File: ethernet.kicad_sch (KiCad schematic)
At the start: 48 parts

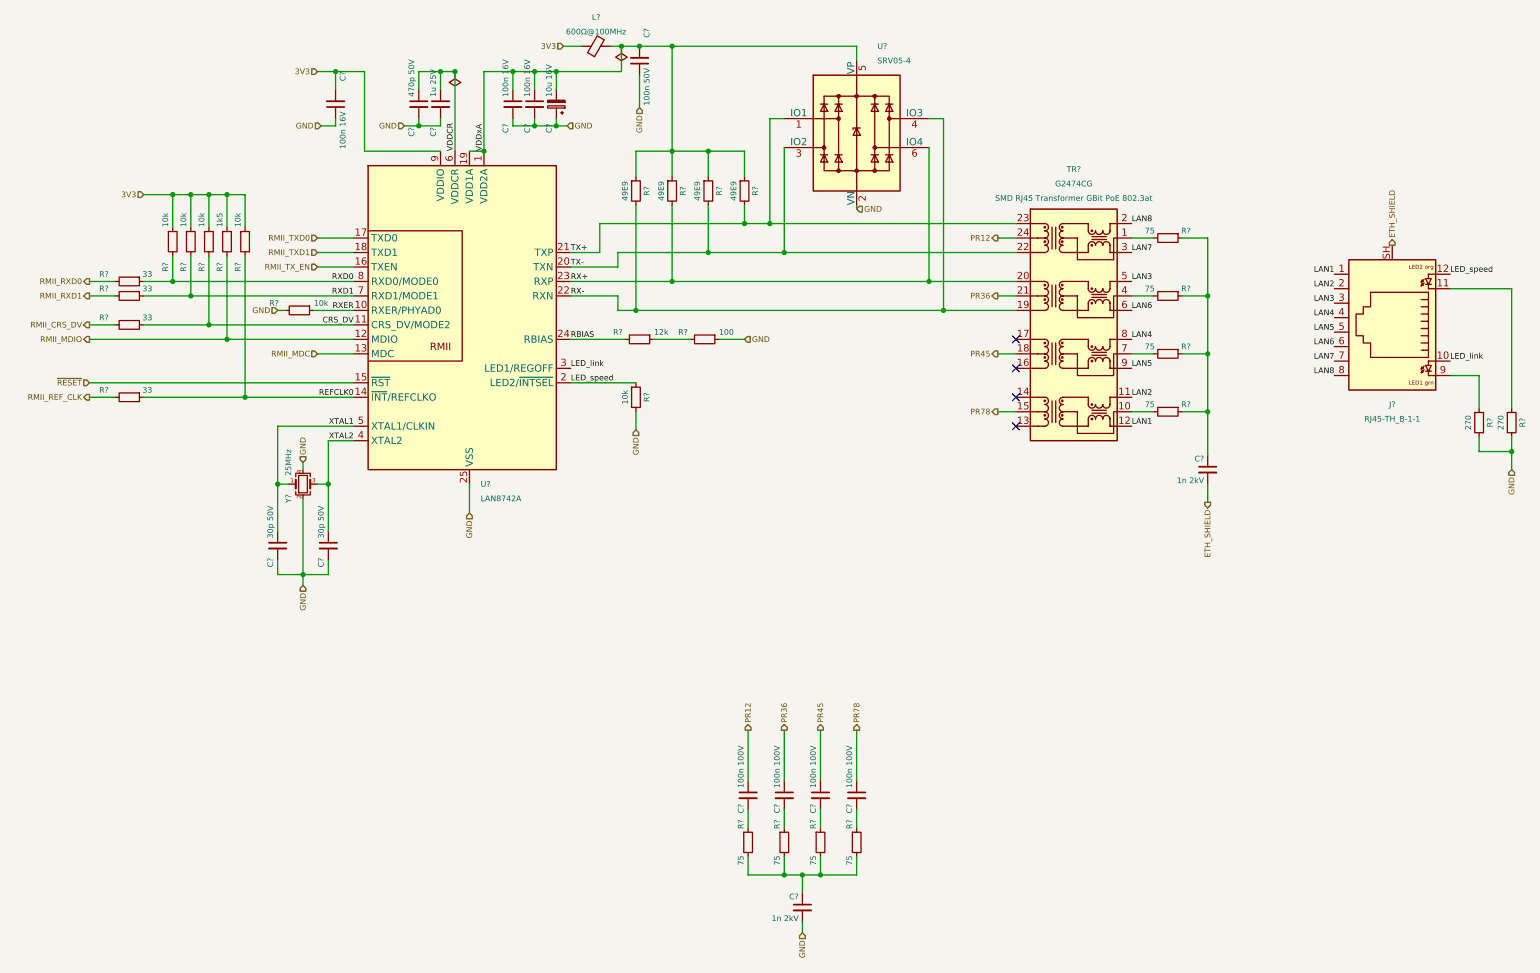
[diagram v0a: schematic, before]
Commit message: Replace transformer, replace RJ45 3D model
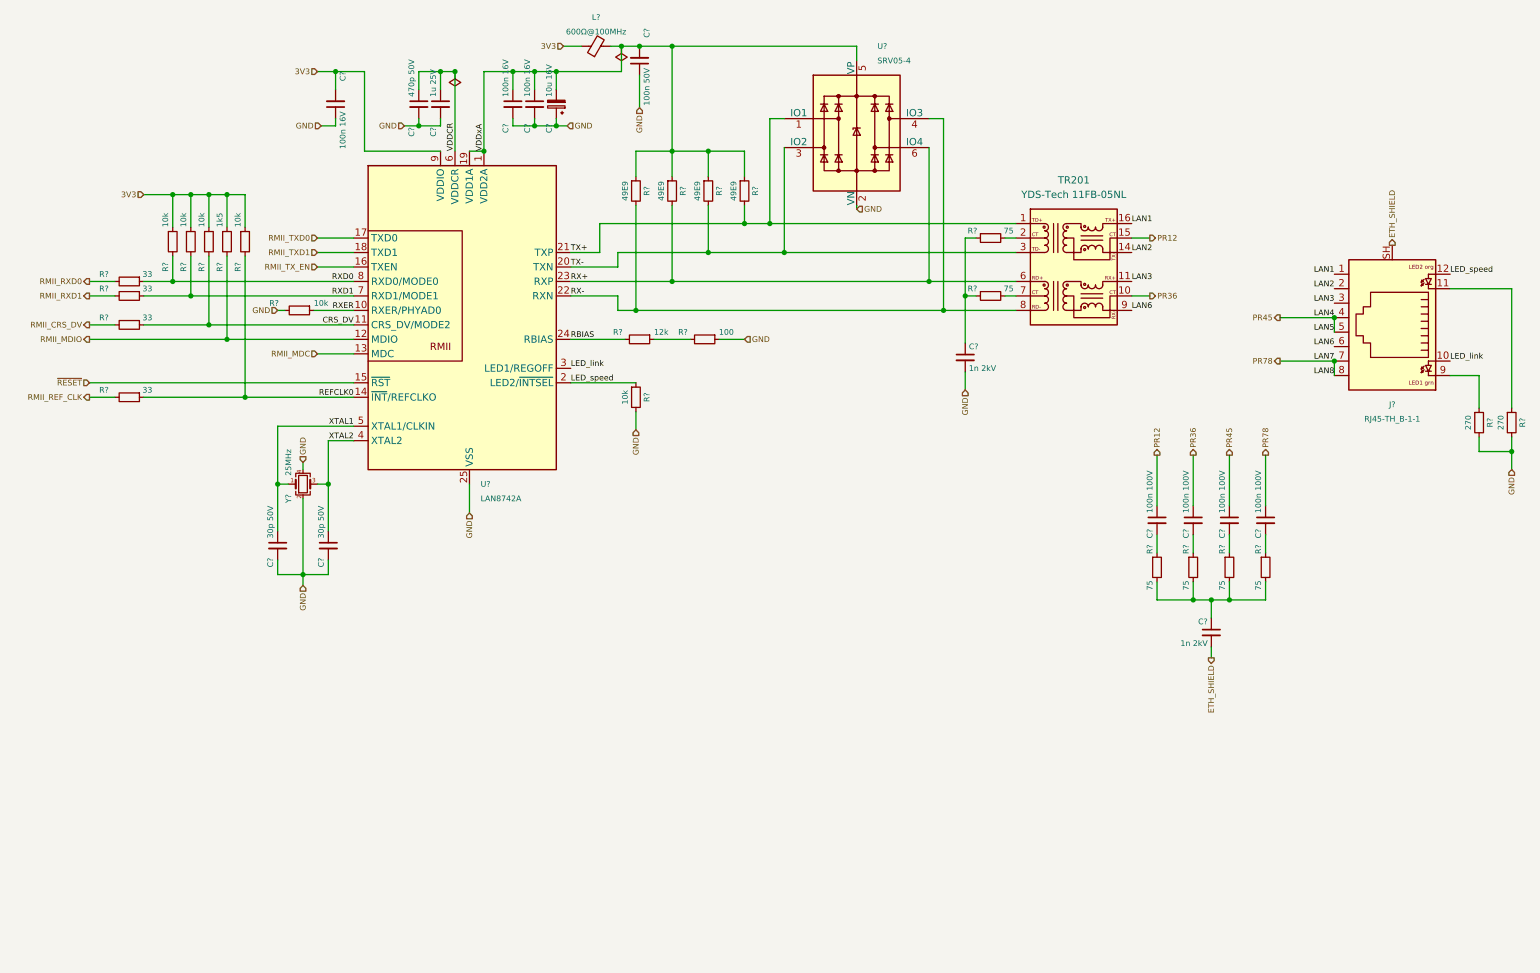
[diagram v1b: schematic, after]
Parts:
- removed R? (x2): 75, Resistor_SMD:R_0603_1608Metric, symbol Device:R_Small
- removed TR?: G2474CG, Project_Library:Mentech G2474CG 24pin 17.2mmx13.97mm, symbol Project_Library:Mentech G2474CG
- added TR201: YDS-Tech 11FB-05NL, Project_Library:YDS-Tech 11FB-05NL, symbol Project_Library:YDS-Tech 11FB-05NL
- J?: footprint Project_Library:RJ45-TH_B-1-1 -> Project_Library:Boomele RJ45-TH_B-1-1
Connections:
- net LAN4 is gone; now on net PR45: J?.4
- net LAN5 is gone; now on net PR45: J?.5
- net LAN7 is gone; now on net PR78: J?.7
- net LAN8 is gone; now on net PR78: J?.8
- net ETH_SHIELD: now also C?.2; no longer C?.2
- net GND: now also C?.2; no longer C?.2
- net LAN1: now also TR201.16 (TD-)
- net LAN2: now also TR201.14 (TD+)
- net LAN3: now also TR201.11 (RD-)
- net LAN6: now also TR201.9 (RD+)
- net PR12: now also TR201.15 (C_TD)
- net PR36: now also TR201.10 (C_RD)
- net RX+: now also TR201.6 (RX-)
- net RX-: now also TR201.8 (RX+)
- net TX+: now also TR201.1 (TX-)
- net TX-: now also TR201.3 (TX+)
- net at R?.2: now also TR201.2 (C_TX)
- net at R?.2: now also TR201.7 (C_RX)
- no-connect marks 4 -> 0
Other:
- moved on the sheet: C?, R?

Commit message: Change LAN footprint
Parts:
- U?: footprint Package_DFN_QFN:VQFN-24-1EP_4x4mm_P0.5mm_EP2.5x2.5mm_ThermalVias -> Package_DFN_QFN:VQFN-24-1EP_4x4mm_P0.5mm_EP2.45x2.45mm_ThermalVias
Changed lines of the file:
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@@
       (effects (font (size 1 1)) (justify left))
     )
-    (property "Footprint" "Package_DFN_QFN:VQFN-24-1EP_4x4mm_P0.5mm_EP2.5x2.5mm_ThermalVias" (at 98.425 107.95 0)
+    (property "Footprint" "Package_DFN_QFN:VQFN-24-1EP_4x4mm_P0.5mm_EP2.45x2.45mm_ThermalVias" (at 98.425 107.95 0)
       (effects (font (size 1 1)) (justify left) hide)
     )

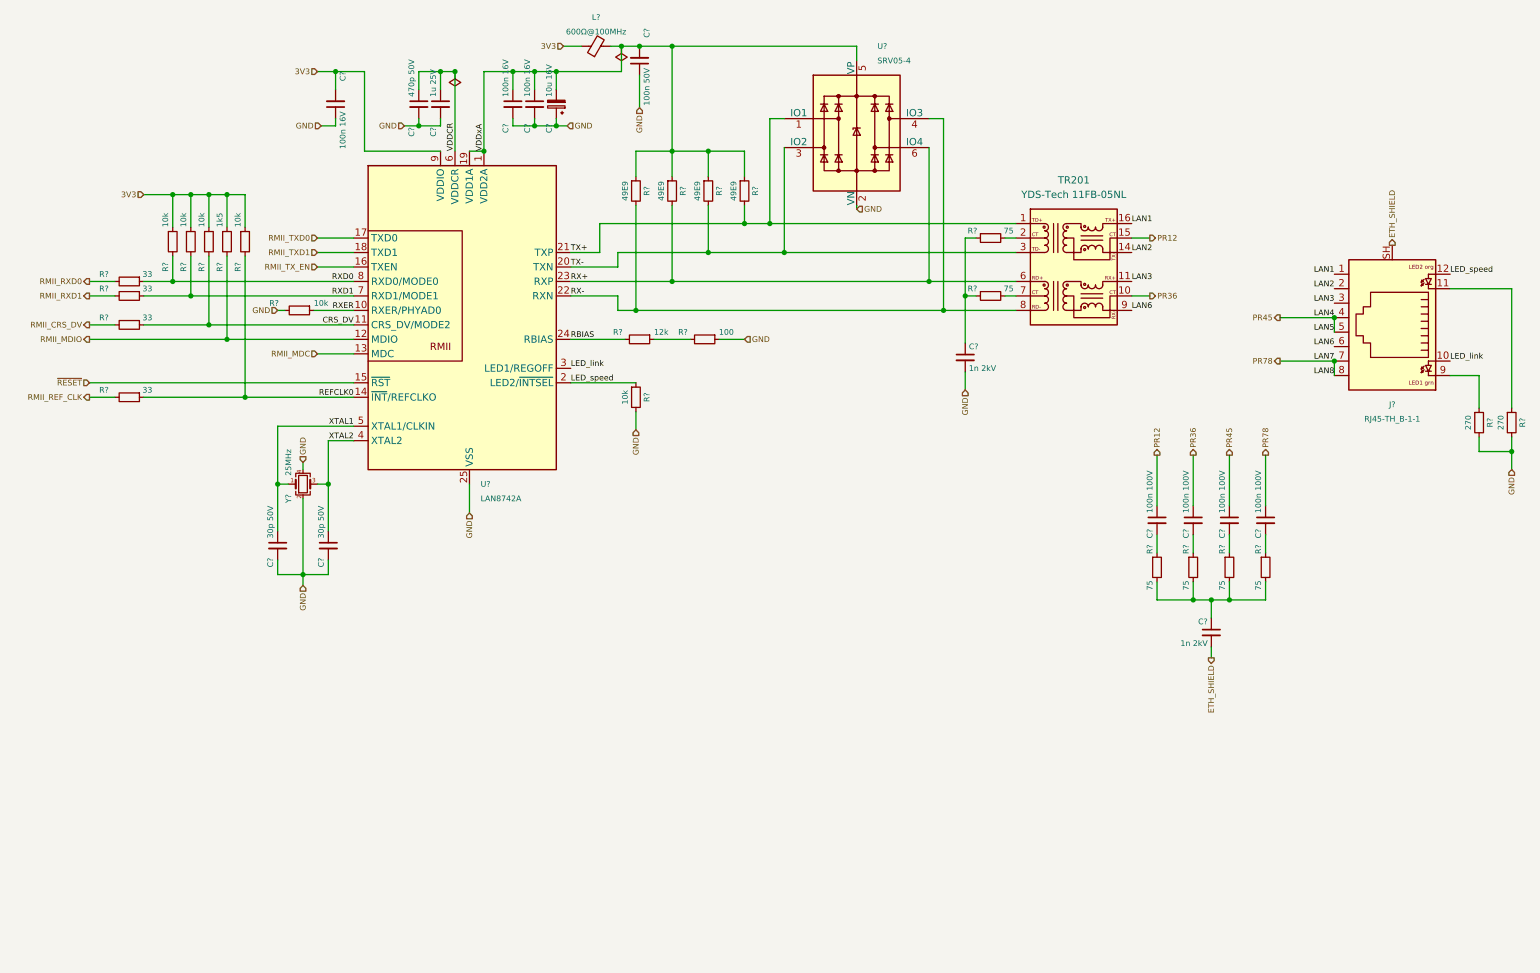
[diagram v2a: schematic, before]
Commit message: Add ETH_RXER
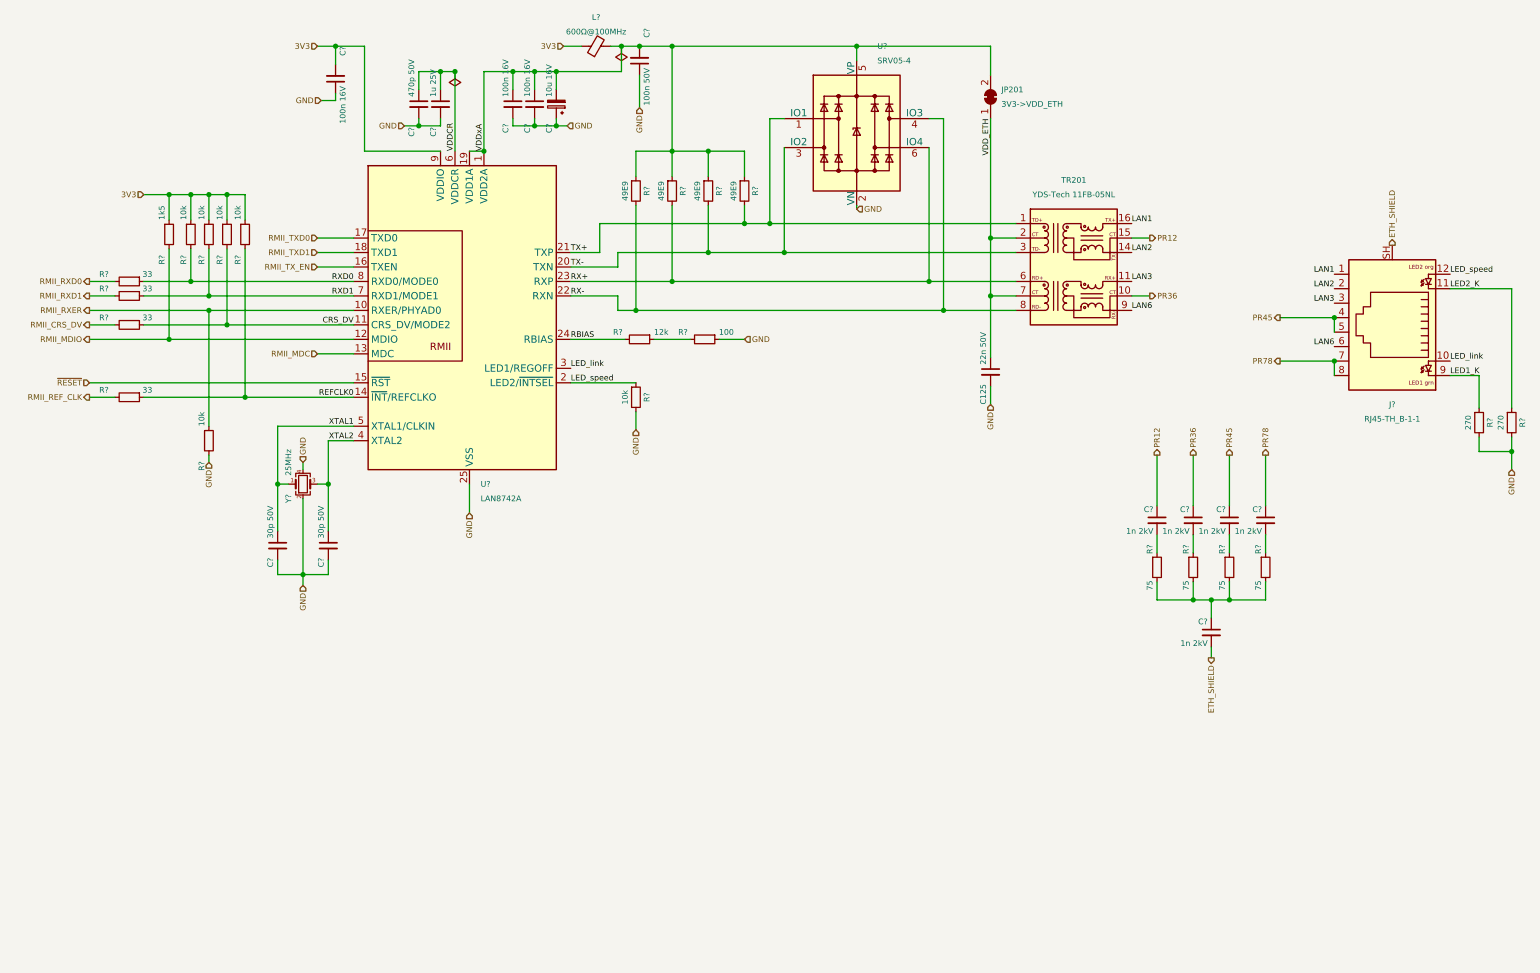
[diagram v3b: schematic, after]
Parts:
- removed C? (x4): 100n 100V, Capacitor_SMD:C_0603_1608Metric, symbol Device:C_Small
- removed C?: 1n 2kV, Capacitor_SMD:C_1206_3216Metric, symbol Device:C_Small
- removed R? (x2): 75, Resistor_SMD:R_0603_1608Metric, symbol Device:R_Small
- added C125: 22n 50V, Capacitor_SMD:C_0603_1608Metric, symbol Device:C_Small
- added C? (x4): 1n 2kV, Capacitor_SMD:C_1206_3216Metric, symbol Device:C_Small
- added JP201: 3V3->VDD_ETH, Jumper:SolderJumper-2_P1.3mm_Bridged_RoundedPad1.0x1.5mm, symbol Jumper:SolderJumper_2_Bridged
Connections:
- net GND: now also C125.2
- net PR12: now also C?.1
- net PR36: now also C?.1
- net PR45: now also C?.1
- net PR78: now also C?.1
- net VDDxA: now also JP201.2 (B)
- net at R?.1: now also C?.2 (x4)
- net VDD_ETH: now reaches TR201.2 (C_TX)
- net VDD_ETH: now also TR201.7 (C_RX), C125.1, JP201.1 (A)
- net LED1_K: now reaches J?.9, R?.1
- net LED2_K: now reaches J?.11, R?.1
- net RXER renamed RMII_RXER
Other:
- moved on the sheet: C?, R?

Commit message: Set DNP
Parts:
- JP201: now left out of the parts list
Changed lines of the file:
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@@
   )
   (symbol (lib_id "Jumper:SolderJumper_2_Bridged") (at 188.595 41.275 90) (unit 1)
-    (in_bom yes) (on_board yes) (dnp no) (fields_autoplaced)
+    (in_bom no) (on_board yes) (dnp no) (fields_autoplaced)
     (property "Reference" "JP201" (at 190.5 40.0049 90)
       (effects (font (size 1 1)) (justify right))
@@
       (effects (font (size 1 1)) hide)
     )
-    (property "Datasheet" "~" (at 119.38 32.385 0)
-      (effects (font (size 1 1)) hide)
-    )
-    (property "Description" "300mΩ ±25% 600Ω@100MHz 0805  Ferrite Beads ROHS" (at 119.38 32.385 0)
-      (effects (font (size 1 1)) hide)
-    )
+    (property "Datasheet" "https://datasheet.lcsc.com/lcsc/2109181830_Sunlord-GZ2012D601TF_C1017.pdf" (at 119.38 32.385 0)
+      (effects (font (size 1 1)) hide)
+    )
+    (property "Description" "300mΩ ±25% 600Ω@100MHz 0805 500mA Ferrite Beads ROHS" (at 119.38 32.385 0)
+      (effects (font (size 1 1)) hide)
+    )

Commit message: #1 Use new central library KiCad-Lib
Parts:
- J?: footprint Project_Library:Boomele RJ45-TH_B-1-1 -> #Connector:Boomele RJ45-TH_B-1-1; symbol Project_Library:Boomele RJ45-TH_B-1-1 -> #Connector:Boomele RJ45-TH_B-1-1
- TR201: footprint Project_Library:YDS-Tech 11FB-05NL -> #Transformer:YDS-Tech 11FB-05NL; symbol Project_Library:YDS-Tech 11FB-05NL -> #Transformer:YDS-Tech 11FB-05NL
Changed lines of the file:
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@@
     )
   )
-  (symbol (lib_id "Project_Library:YDS-Tech 11FB-05NL") (at 203.2 71.12 0) (unit 1)
+  (symbol (lib_id "#Transformer:YDS-Tech 11FB-05NL") (at 203.2 71.12 0) (unit 1)
     (in_bom yes) (on_board yes) (dnp no) (fields_autoplaced)
     (property "Reference" "TR201" (at 203.2 55.88 0)
@@
       (effects (font (size 1 1)))
     )
-    (property "Footprint" "Project_Library:YDS-Tech 11FB-05NL" (at 203.2 92.71 0)
-      (effects (font (size 1 1)) hide)
-    )
-    (property "Datasheet" "https://datasheet.lcsc.com/lcsc/1811151534_Shanghai-YDS-Tech-11FB-05NL_C97692.pdf" (at 203.2 49.53 0)
-      (effects (font (size 1 1)) hide)
+    (property "Footprint" "#Transformer:YDS-Tech 11FB-05NL" (at 203.2 92.71 0)
+      (effects (font (size 1.27 1.27)) hide)
+    )
+    (property "Datasheet" "${KIPRJMOD}/KiCad-Lib/#Transformer.doc/YDS-Tech 11FB-05NL.pdf" (at 203.2 49.53 0)
+      (effects (font (size 1.27 1.27)) hide)
     )
     (property "Manufacturer" "Shanghai YDS Tech" (at 203.2 86.36 0)
-      (effects (font (size 1 1)) hide)
+      (effects (font (size 1.27 1.27)) hide)
     )
     (property "Partnumber" "11FB-05NL" (at 203.2 92.71 0)
-      (effects (font (size 1 1)) hide)
+      (effects (font (size 1.27 1.27)) hide)
     )
     (property "JLCPCB Part #" "C97692" (at 203.2 85.09 0) (show_name)
-      (effects (font (size 1 1)) hide)
+      (effects (font (size 1.27 1.27)) hide)
     )
     (property "Description" "Ethernet LAN 10/100 Base-Tx Transformer, PoE 350mA" (at 203.2 58.42 0)
-      (effects (font (size 1 1)) hide)
+      (effects (font (size 1.27 1.27)) hide)
     )
     (property "isBasicPart" "NO" (at 203.2 95.25 0) (show_name)
-      (effects (font (size 1 1)) hide)
+      (effects (font (size 1.27 1.27)) hide)
     )
     (pin "1")
@@
     )
   )
-  (symbol (lib_id "Project_Library:Boomele RJ45-TH_B-1-1") (at 259.08 80.01 180) (unit 1)
+  (symbol (lib_id "#Connector:Boomele RJ45-TH_B-1-1") (at 259.08 80.01 180) (unit 1)
     (in_bom yes) (on_board yes) (dnp no) (fields_autoplaced)
     (property "Reference" "J?" (at 259.08 95.25 0)
@@
       (effects (font (size 1 1)))
     )
-    (property "Footprint" "Project_Library:Boomele RJ45-TH_B-1-1" (at 259.08 63.5 0)
-      (effects (font (size 1 1)) hide)
-    )
-    (property "Datasheet" "https://datasheet.lcsc.com/lcsc/1811141116_BOOMELE-Boom-Precision-Elec-RJ45-B-1-1_C138392.pdf" (at 259.08 60.96 0)
-      (effects (font (size 1 1)) hide)
+    (property "Footprint" "#Connector:Boomele RJ45-TH_B-1-1" (at 259.08 63.5 0)
+      (effects (font (size 1.27 1.27)) hide)
+    )
+    (property "Datasheet" "${KIPRJMOD}/KiCad-Lib/#Connector.doc/Boomele RJ45-TH_B-1-1.pdf" (at 259.08 60.96 0)
+      (effects (font (size 1.27 1.27)) hide)
     )
     (property "Description" "RJ45 RJReceptacle 1 Plugin  Ethernet Connectors/Modular Connectors (RJ45 RJ11) ROHS" (at 259.08 66.04 0)
-      (effects (font (size 1 1)) hide)
+      (effects (font (size 1.27 1.27)) hide)
     )
     (property "Partnumber" "RJ45-B-1*1" (at 259.08 99.06 0)
-      (effects (font (size 1 1)) hide)
+      (effects (font (size 1.27 1.27)) hide)
     )
     (property "JLCPCB Part #" "C138392" (at 259.08 104.14 0) (show_name)
-      (effects (font (size 1 1)) hide)
+      (effects (font (size 1.27 1.27)) hide)
     )
     (property "isBasicPart" "NO" (at 259.08 101.6 0) (show_name)
-      (effects (font (size 1 1)) hide)
+      (effects (font (size 1.27 1.27)) hide)
     )
     (property "Manufacturer" "BOOMELE(Boom Precision Elec)" (at 259.08 96.52 0)
-      (effects (font (size 1 1)) hide)
-    )
-    (pin "1")
+      (effects (font (size 1.27 1.27)) hide)
+    )
+    (pin "1")

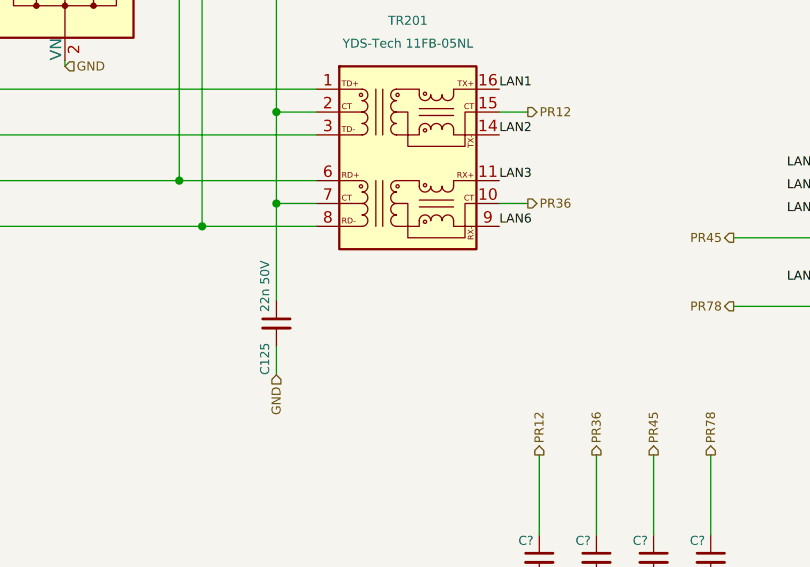
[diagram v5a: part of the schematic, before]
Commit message: Move PoE pin socket and add earth zone
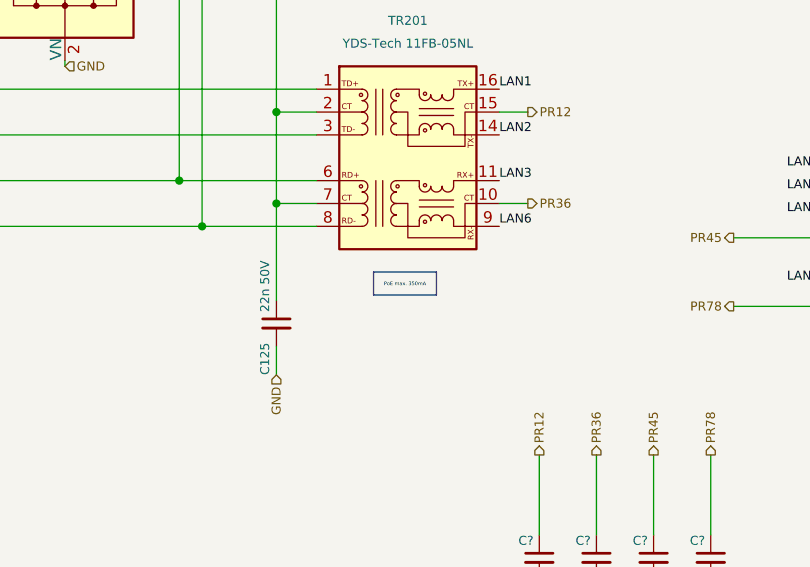
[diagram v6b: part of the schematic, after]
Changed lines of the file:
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@@
     (stroke (width 0) (type default))
+  )
+  (text_box "PoE max. 350mA"
+    (at 199.39 83.82 0) (size 6.985 2.54)
+    (stroke (width 0.01) (type default) (color 255 0 0 1))
+    (fill (type color) (color 255 255 194 1))
+    (effects (font (face "Input Sans Compressed") (size 0.4 0.4) (color 255 0 0 1)))
   )
   (label "LED2_K" (at 269.24 74.93 0) (fields_autoplaced)

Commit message: #2 Add silkscreen texts
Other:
- company: (none) -> easy-smart solution GmbH
- title: (none) -> STM32F4 Uno Ethernet
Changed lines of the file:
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@@
 (kicad_sch (version 20230121) (generator eeschema)
   (paper "A4")
+  (title_block
+    (title "STM32F4 Uno Ethernet")
+    (date "2023-10-02")
+    (rev "1.0.x-dev")
+    (company "easy-smart solution GmbH")
+  )
   (junction (at 57.785 93.98) (diameter 0) (color 0 0 0 0)
   )
